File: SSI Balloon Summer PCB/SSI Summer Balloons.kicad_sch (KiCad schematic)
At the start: 0 parts

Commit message: Finished GPS
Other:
- sheet GPS ports: added +3V3, GND, GPS_RX, GPS_TX; removed none
- sheet Power ports: added none; removed +1V8
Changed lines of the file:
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@@
+	)
+	(junction
+		(at 99.06 69.85)
+		(diameter 0)
+		(color 0 0 0 0)
 	)
 	(junction
@@
 	)
 	(junction
-		(at 98.425 69.85)
-		(diameter 0)
-		(color 0 0 0 0)
-	)
-	(junction
 		(at 207.01 58.42)
 		(diameter 0)
@@
 	(wire
 		(pts
+			(xy 99.06 69.85) (xy 99.06 120.65)
+		)
+		(stroke
+			(width 0)
+			(type default)
+		)
+	)
+	(wire
+		(pts
 			(xy 209.55 95.25) (xy 180.34 95.25)
 		)
@@
 	(wire
 		(pts
+			(xy 93.98 120.65) (xy 93.98 116.84)
+		)
+		(stroke
+			(width 0)
+			(type default)
+		)
+	)
+	(wire
+		(pts
+			(xy 113.03 116.84) (xy 113.03 55.88)
+		)
+		(stroke
+			(width 0)
+			(type default)
+		)
+	)
+	(wire
+		(pts
+			(xy 90.17 114.3) (xy 110.49 114.3)
+		)
+		(stroke
+			(width 0)
+			(type default)
+		)
+	)
+	(wire
+		(pts
 			(xy 207.01 92.71) (xy 177.8 92.71)
 		)
@@
 	(wire
 		(pts
+			(xy 99.06 69.85) (xy 116.84 69.85)
+		)
+		(stroke
+			(width 0)
+			(type default)
+		)
+	)
+	(wire
+		(pts
+			(xy 110.49 114.3) (xy 110.49 53.34)
+		)
+		(stroke
+			(width 0)
+			(type default)
+		)
+	)
+	(wire
+		(pts
 			(xy 207.01 58.42) (xy 207.01 92.71)
 		)
@@
 	(wire
 		(pts
+			(xy 110.49 53.34) (xy 116.84 53.34)
+		)
+		(stroke
+			(width 0)
+			(type default)
+		)
+	)
+	(wire
+		(pts
 			(xy 153.67 76.2) (xy 153.67 120.65)
 		)
@@
 	(wire
 		(pts
+			(xy 113.03 55.88) (xy 116.84 55.88)
+		)
+		(stroke
+			(width 0)
+			(type default)
+		)
+	)
+	(wire
+		(pts
 			(xy 191.77 38.1) (xy 223.52 38.1)
 		)
@@
 	(wire
 		(pts
-			(xy 97.79 69.85) (xy 98.425 69.85)
+			(xy 97.155 69.85) (xy 99.06 69.85)
 		)
 		(stroke
@@
 	(wire
 		(pts
+			(xy 43.18 76.2) (xy 43.18 78.74)
+		)
+		(stroke
+			(width 0)
+			(type default)
+		)
+	)
+	(wire
+		(pts
+			(xy 43.18 118.11) (xy 43.18 120.65)
+		)
+		(stroke
+			(width 0)
+			(type default)
+		)
+	)
+	(wire
+		(pts
 			(xy 191.77 54.61) (xy 209.55 54.61)
 		)
@@
 	(wire
 		(pts
-			(xy 98.425 69.85) (xy 116.84 69.85)
+			(xy 93.98 116.84) (xy 113.03 116.84)
 		)
 		(stroke
@@
 	(wire
 		(pts
+			(xy 90.17 120.65) (xy 90.17 114.3)
+		)
+		(stroke
+			(width 0)
+			(type default)
+		)
+	)
+	(wire
+		(pts
 			(xy 158.75 76.2) (xy 158.75 120.65)
 		)
@@
 			(width 0)
 			(type default)
+		)
+	)
+	(global_label "GND"
+		(shape input)
+		(at 43.18 78.74 270)
+		(fields_autoplaced yes)
+		(effects
+			(font
+				(size 1.27 1.27)
+			)
+			(justify right)
+		)
+		(property "Intersheetrefs" "${INTERSHEET_REFS}"
+			(at 43.18 85.5957 90)
+			(hide yes)
+			(show_name no)
+			(do_not_autoplace no)
+			(effects
+				(font
+					(size 1.27 1.27)
+				)
+				(justify right)
+			)
+		)
+	)
+	(global_label "GND"
+		(shape input)
+		(at 43.18 118.11 90)
+		(fields_autoplaced yes)
+		(effects
+			(font
+				(size 1.27 1.27)
+			)
+			(justify left)
+		)
+		(property "Intersheetrefs" "${INTERSHEET_REFS}"
+			(at 43.18 111.2543 90)
+			(hide yes)
+			(show_name no)
+			(do_not_autoplace no)
+			(effects
+				(font
+					(size 1.27 1.27)
+				)
+				(justify left)
+			)
 		)
 	)
@@
 	(sheet
 		(at 20.32 120.65)
-		(size 78.105 38.735)
+		(size 80.264 38.735)
 		(exclude_from_sim no)
 		(in_bom yes)
@@
 		)
 		(property "Sheetname" "GPS"
-			(at 20.32 119.9384 0)
+			(at 19.6084 159.385 90)
 			(show_name no)
 			(do_not_autoplace no)
@@
 		)
 		(property "Sheetfile" "GPS.kicad_sch"
-			(at 20.32 159.9696 0)
+			(at 101.1686 159.385 90)
 			(show_name no)
 			(do_not_autoplace no)
@@
 				)
 				(justify left top)
+			)
+		)
+		(pin "+3V3" input
+			(at 99.06 120.65 90)
+			(effects
+				(font
+					(size 1.27 1.27)
+				)
+				(justify right)
+			)
+		)
+		(pin "GND" passive
+			(at 43.18 120.65 90)
+			(effects
+				(font
+					(size 1.27 1.27)
+				)
+				(justify right)
+			)
+		)
+		(pin "GPS_RX" input
+			(at 90.17 120.65 90)
+			(effects
+				(font
+					(size 1.27 1.27)
+				)
+				(justify right)
+			)
+		)
+		(pin "GPS_TX" output
+			(at 93.98 120.65 90)
+			(effects
+				(font
+					(size 1.27 1.27)
+				)
+				(justify right)
 			)
 		)
@@
 	)
 	(sheet
-		(at 20.32 34.29)
+		(at 19.05 34.29)
 		(size 78.105 41.91)
 		(exclude_from_sim no)
@@
 		)
 		(property "Sheetname" "Power"
-			(at 20.32 33.5784 0)
+			(at 19.05 33.5784 0)
 			(show_name no)
 			(do_not_autoplace no)
@@
 		)
 		(property "Sheetfile" "Power.kicad_sch"
-			(at 20.32 76.7846 0)
+			(at 19.05 76.7846 0)
 			(show_name no)
 			(do_not_autoplace no)
@@
 			)
 		)
-		(pin "+1V8" output
-			(at 50.8 76.2 270)
-			(effects
-				(font
-					(size 1.27 1.27)
-				)
-				(justify left)
-			)
-		)
 		(pin "+3V3" output
-			(at 98.425 69.85 0)
+			(at 97.155 69.85 0)
 			(effects
 				(font
@@
 		)
 		(pin "GND" passive
-			(at 20.32 42.545 180)
+			(at 43.18 76.2 270)
 			(effects
 				(font
@@
 		)
 		(pin "+4V1" output
-			(at 87.63 76.2 270)
+			(at 86.36 76.2 270)
 			(effects
 				(font
@@
 			)
 		)
-		(pin "GPS_RX" input
+		(pin "GPS_RX" output
 			(at 116.84 53.34 180)
 			(effects
@@
 			)
 		)
-		(pin "APRS_RX" input
+		(pin "APRS_RX" output
 			(at 167.64 76.2 270)
 			(effects
@@
 			)
 		)
-		(pin "GPS_TX" output
+		(pin "GPS_TX" input
 			(at 116.84 55.88 180)
 			(effects
@@
 			)
 		)
-		(pin "APRS_TX" output
+		(pin "APRS_TX" input
 			(at 170.18 76.2 270)
 			(effects

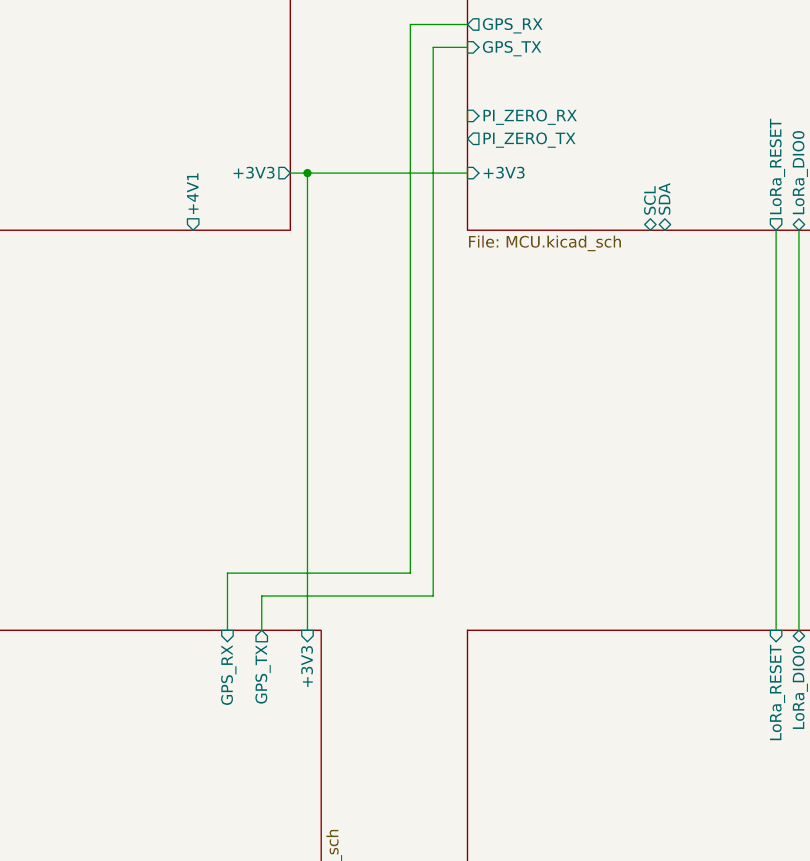
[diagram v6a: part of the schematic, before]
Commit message: Tidied some labels up
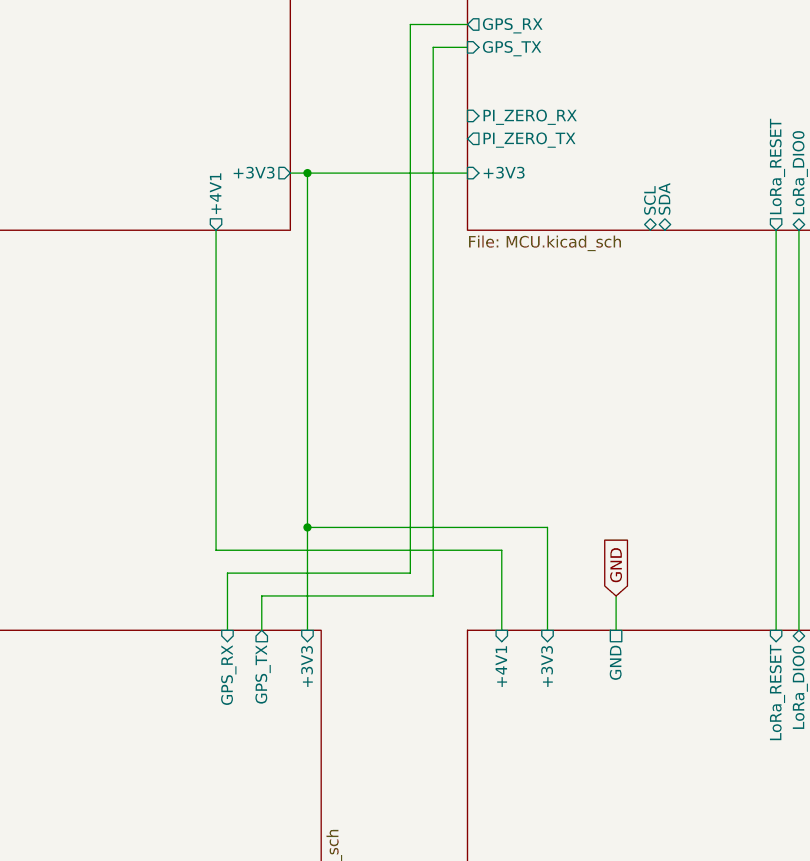
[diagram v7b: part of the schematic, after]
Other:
- sheet Radio ports: added +3V3, +4V1, GND; removed none
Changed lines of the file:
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@@
+	)
+	(junction
+		(at 99.06 109.22)
+		(diameter 0)
+		(color 0 0 0 0)
 	)
 	(junction
@@
 	(wire
 		(pts
-			(xy 99.06 69.85) (xy 99.06 120.65)
-		)
-		(stroke
-			(width 0)
-			(type default)
-		)
-	)
-	(wire
-		(pts
 			(xy 209.55 95.25) (xy 180.34 95.25)
 		)
@@
 	(wire
 		(pts
+			(xy 120.65 111.76) (xy 88.9 111.76)
+		)
+		(stroke
+			(width 0)
+			(type default)
+		)
+	)
+	(wire
+		(pts
 			(xy 177.8 92.71) (xy 177.8 120.65)
 		)
@@
 	(wire
 		(pts
+			(xy 125.73 120.65) (xy 125.73 109.22)
+		)
+		(stroke
+			(width 0)
+			(type default)
+		)
+	)
+	(wire
+		(pts
 			(xy 172.72 76.2) (xy 172.72 120.65)
 		)
@@
 	(wire
 		(pts
+			(xy 133.35 116.84) (xy 133.35 120.65)
+		)
+		(stroke
+			(width 0)
+			(type default)
+		)
+	)
+	(wire
+		(pts
 			(xy 207.01 58.42) (xy 223.52 58.42)
 		)
@@
 	(wire
 		(pts
+			(xy 125.73 109.22) (xy 99.06 109.22)
+		)
+		(stroke
+			(width 0)
+			(type default)
+		)
+	)
+	(wire
+		(pts
 			(xy 156.21 76.2) (xy 156.21 120.65)
 		)
@@
 	(wire
 		(pts
+			(xy 99.06 69.85) (xy 99.06 109.22)
+		)
+		(stroke
+			(width 0)
+			(type default)
+		)
+	)
+	(wire
+		(pts
 			(xy 191.77 58.42) (xy 207.01 58.42)
 		)
@@
 	(wire
 		(pts
+			(xy 88.9 111.76) (xy 88.9 76.2)
+		)
+		(stroke
+			(width 0)
+			(type default)
+		)
+	)
+	(wire
+		(pts
 			(xy 191.77 41.91) (xy 223.52 41.91)
 		)
@@
 	(wire
 		(pts
+			(xy 99.06 109.22) (xy 99.06 120.65)
+		)
+		(stroke
+			(width 0)
+			(type default)
+		)
+	)
+	(wire
+		(pts
 			(xy 167.64 76.2) (xy 167.64 120.65)
+		)
+		(stroke
+			(width 0)
+			(type default)
+		)
+	)
+	(wire
+		(pts
+			(xy 120.65 120.65) (xy 120.65 111.76)
 		)
 		(stroke
@@
 		(property "Intersheetrefs" "${INTERSHEET_REFS}"
 			(at 43.18 111.2543 90)
+			(hide yes)
+			(show_name no)
+			(do_not_autoplace no)
+			(effects
+				(font
+					(size 1.27 1.27)
+				)
+				(justify left)
+			)
+		)
+	)
+	(global_label "GND"
+		(shape input)
+		(at 133.35 116.84 90)
+		(fields_autoplaced yes)
+		(effects
+			(font
+				(size 1.27 1.27)
+			)
+			(justify left)
+		)
+		(property "Intersheetrefs" "${INTERSHEET_REFS}"
+			(at 133.35 109.9843 90)
 			(hide yes)
 			(show_name no)
@@
 		)
 		(pin "+4V1" output
-			(at 86.36 76.2 270)
+			(at 88.9 76.2 270)
 			(effects
 				(font
@@
 			(effects
 				(font
+					(size 1.27 1.27)
+				)
+				(justify right)
+			)
+		)
+		(pin "+3V3" input
+			(at 125.73 120.65 90)
+			(effects
+				(font
+					(size 1.27 1.27)
+				)
+				(justify right)
+			)
+		)
+		(pin "+4V1" input
+			(at 120.65 120.65 90)
+			(effects
+				(font
+					(size 1.27 1.27)
+				)
+				(justify right)
+			)
+		)
+		(pin "GND" passive
+			(at 133.35 120.65 90)
+			(effects
+				(font

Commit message: adding IMU footprint+symbol
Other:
- sheet MCU (STM) ports: added GND; removed none
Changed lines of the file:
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@@
+	(wire
+		(pts
+			(xy 144.78 76.2) (xy 144.78 80.01)
+		)
+		(stroke
+			(width 0)
+			(type default)
+		)
+	)
 	(wire
 		(pts
@@
 				)
 				(justify left)
+			)
+		)
+	)
+	(global_label "GND"
+		(shape input)
+		(at 144.78 80.01 270)
+		(fields_autoplaced yes)
+		(effects
+			(font
+				(size 1.27 1.27)
+			)
+			(justify right)
+		)
+		(property "Intersheetrefs" "${INTERSHEET_REFS}"
+			(at 144.78 86.8657 90)
+			(hide yes)
+			(show_name no)
+			(do_not_autoplace no)
+			(effects
+				(font
+					(size 1.27 1.27)
+				)
+				(justify right)
 			)
 		)
@@
 			(effects
 				(font
+					(size 1.27 1.27)
+				)
+				(justify left)
+			)
+		)
+		(pin "GND" passive
+			(at 144.78 76.2 270)
+			(effects
+				(font
